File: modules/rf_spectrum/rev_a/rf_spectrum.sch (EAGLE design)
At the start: 38 parts, among them J1 MODULE_GENERIC_DEBUGSMT, J2 U.FL-R-SMT, J3 U.FL-R-SMT, J4 U.FL-R-SMT, J7 TC2030-JLINK-L, P1 MOLEX_73251-135X, U1 STM32L432KC, U2 MWSUB3G, U3 SKY13317, U7 TLV62130, X2 ABS05-32.768KHZ-9-T

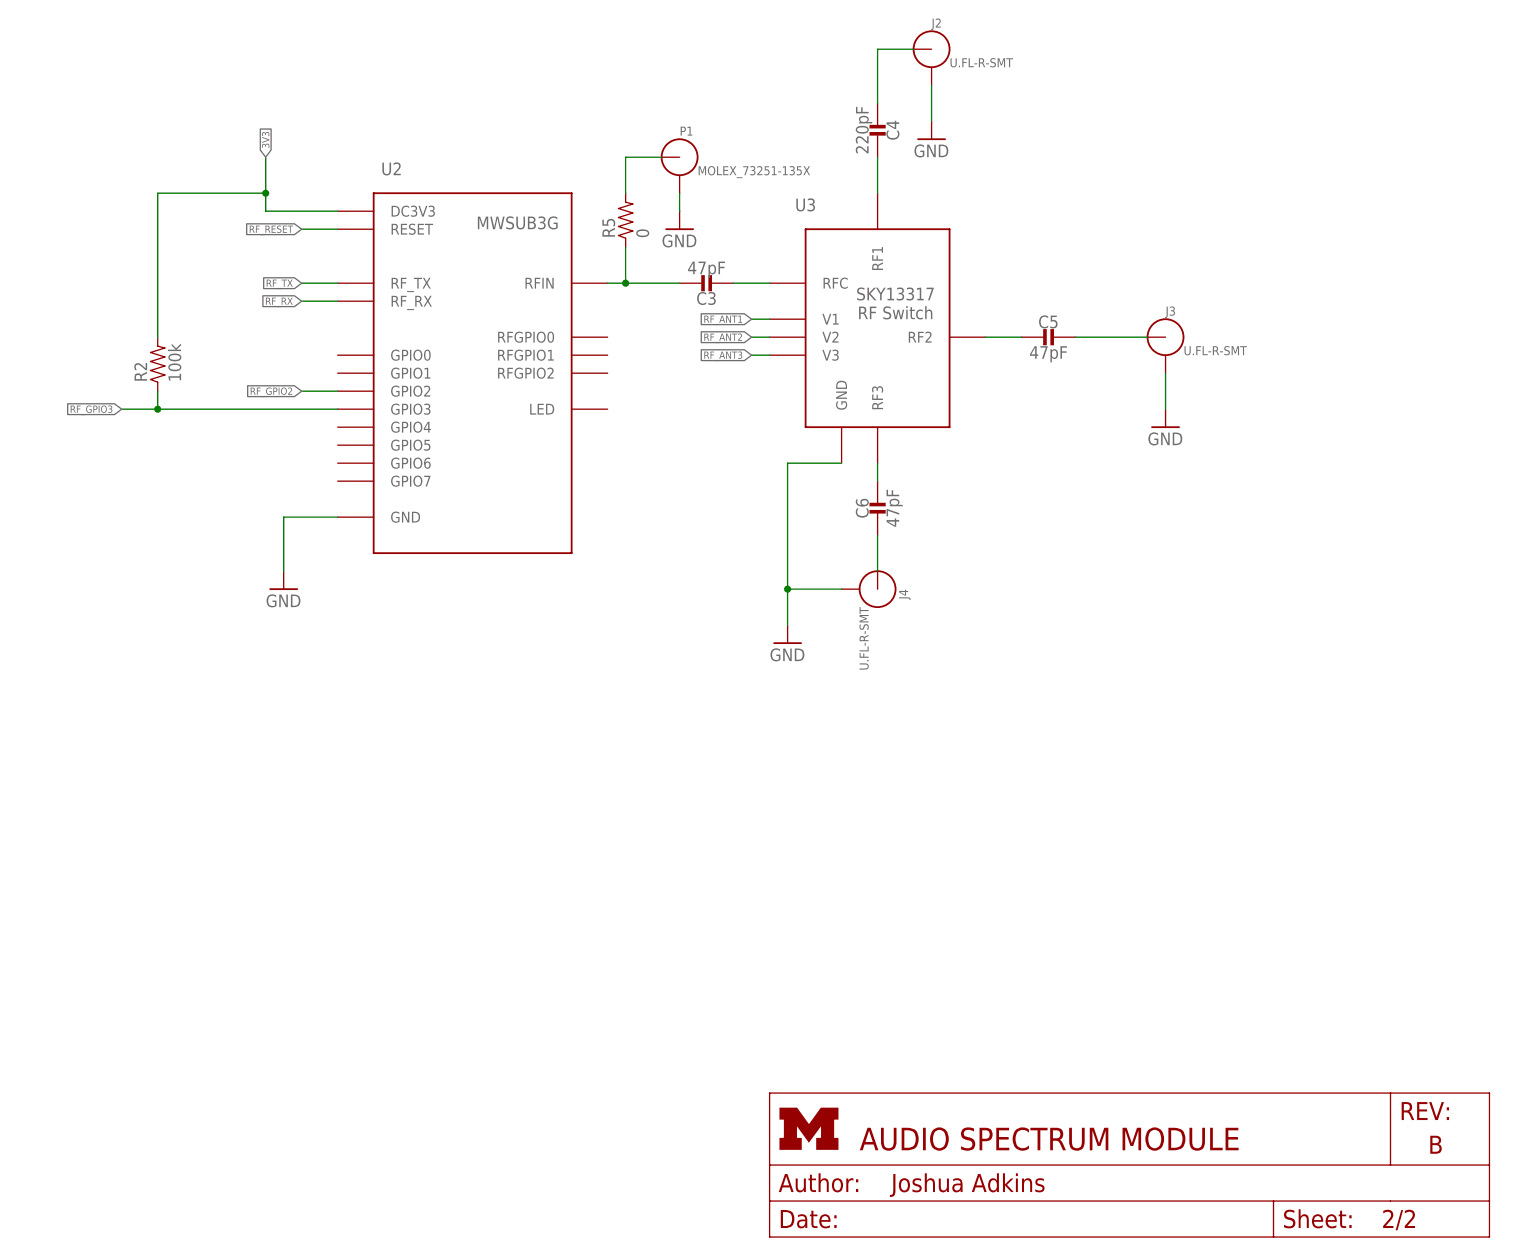
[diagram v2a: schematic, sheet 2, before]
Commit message: added debug signals and better labels
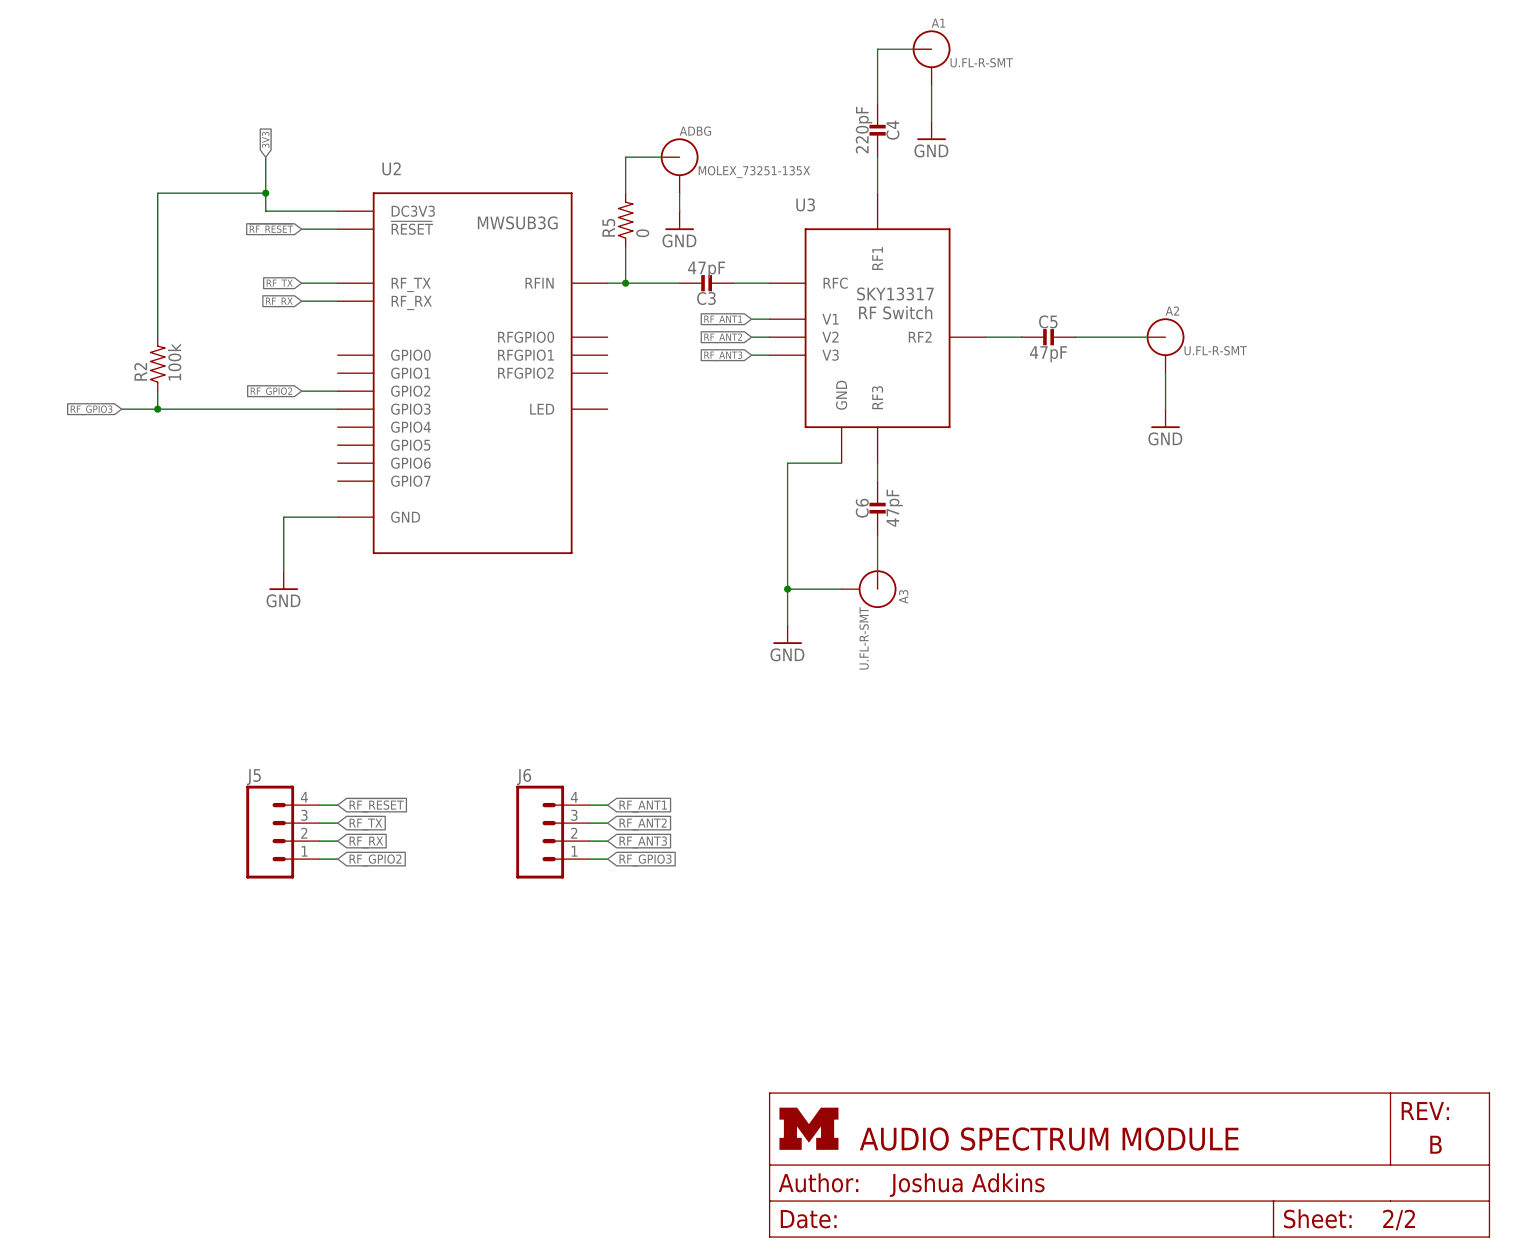
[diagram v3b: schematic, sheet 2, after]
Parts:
- added J5, J6: (no value), SparkFun-Connectors:M04PTH
- renumbered J2 to A1, J3 to A2, J4 to A3, P1 to ADBG
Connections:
- removed net RF_RESET: U1.PA8, U2.RESET
- new net !RF_RESET: J5.4, U1.PA8, U2.!RESET
- net RF_ANT1: now also J6.4
- net RF_ANT2: now also J6.3
- net RF_ANT3: now also J6.2
- net RF_GPIO2: now also J5.1
- net RF_GPIO3: now also J6.1
- net RF_RX: now also J5.2
- net RF_TX: now also J5.3
- net SWDCLK: now also U1.PA14/SWDCLK; no longer U1.PA14/SWCLK

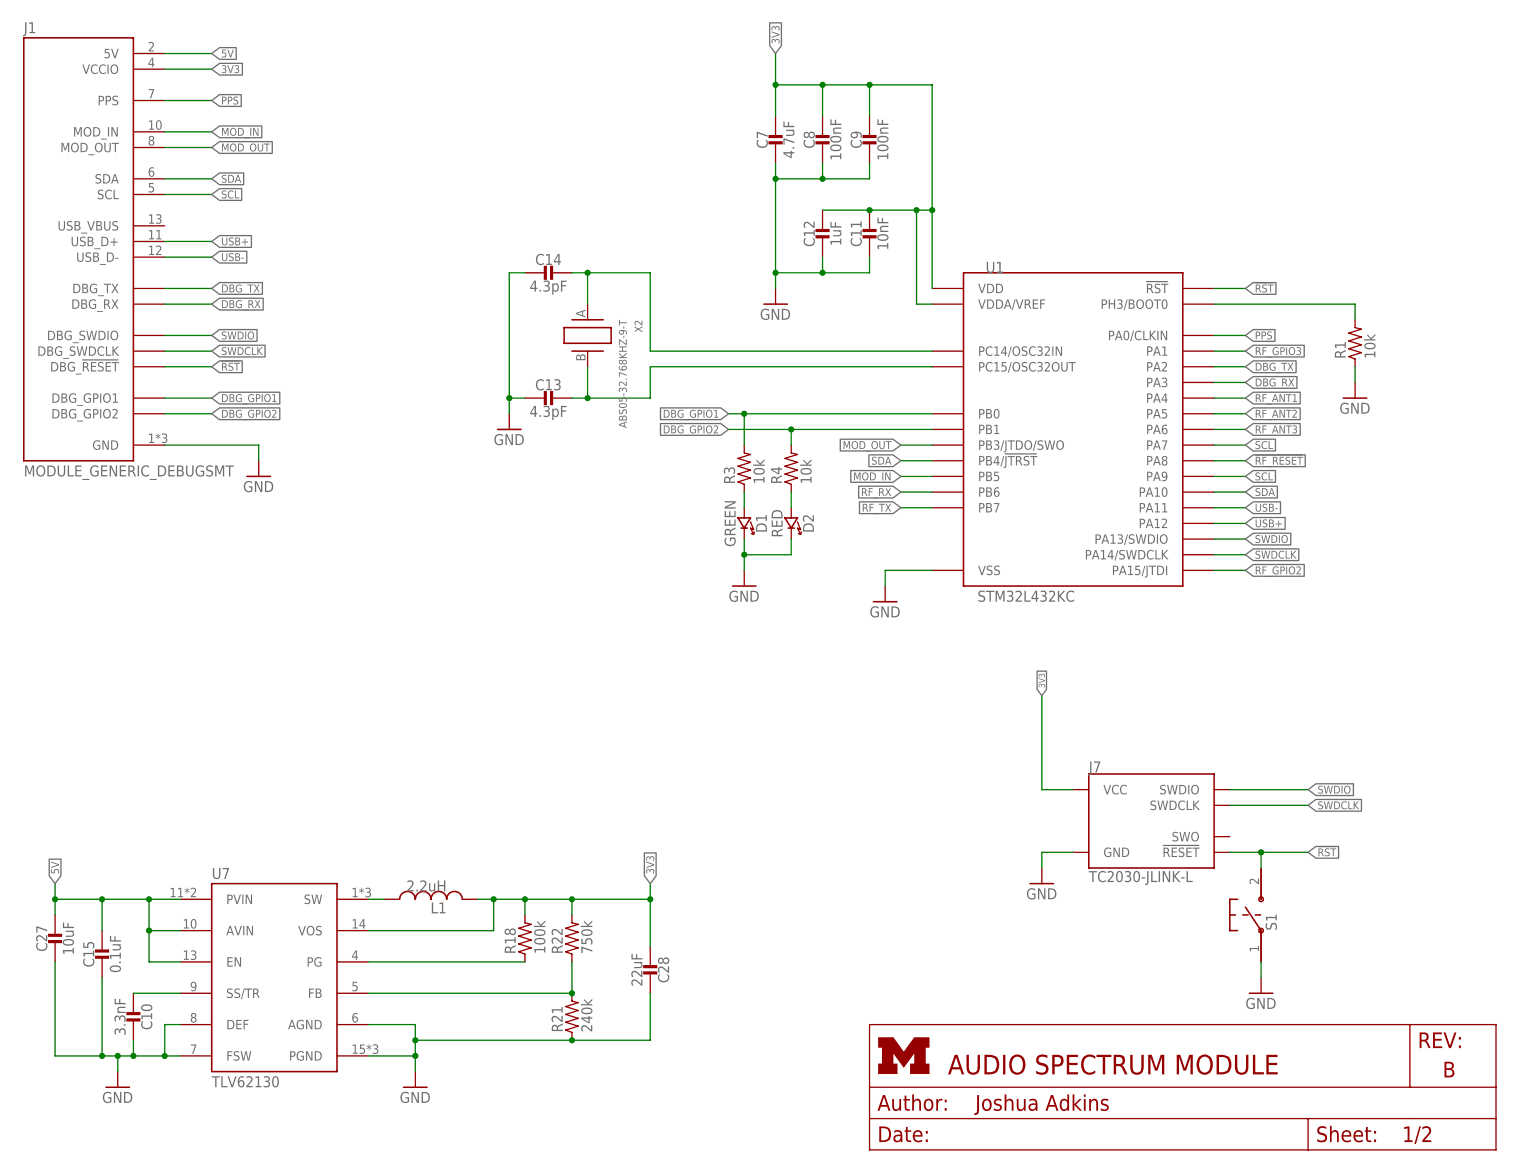
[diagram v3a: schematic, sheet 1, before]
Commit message: renumbered parts
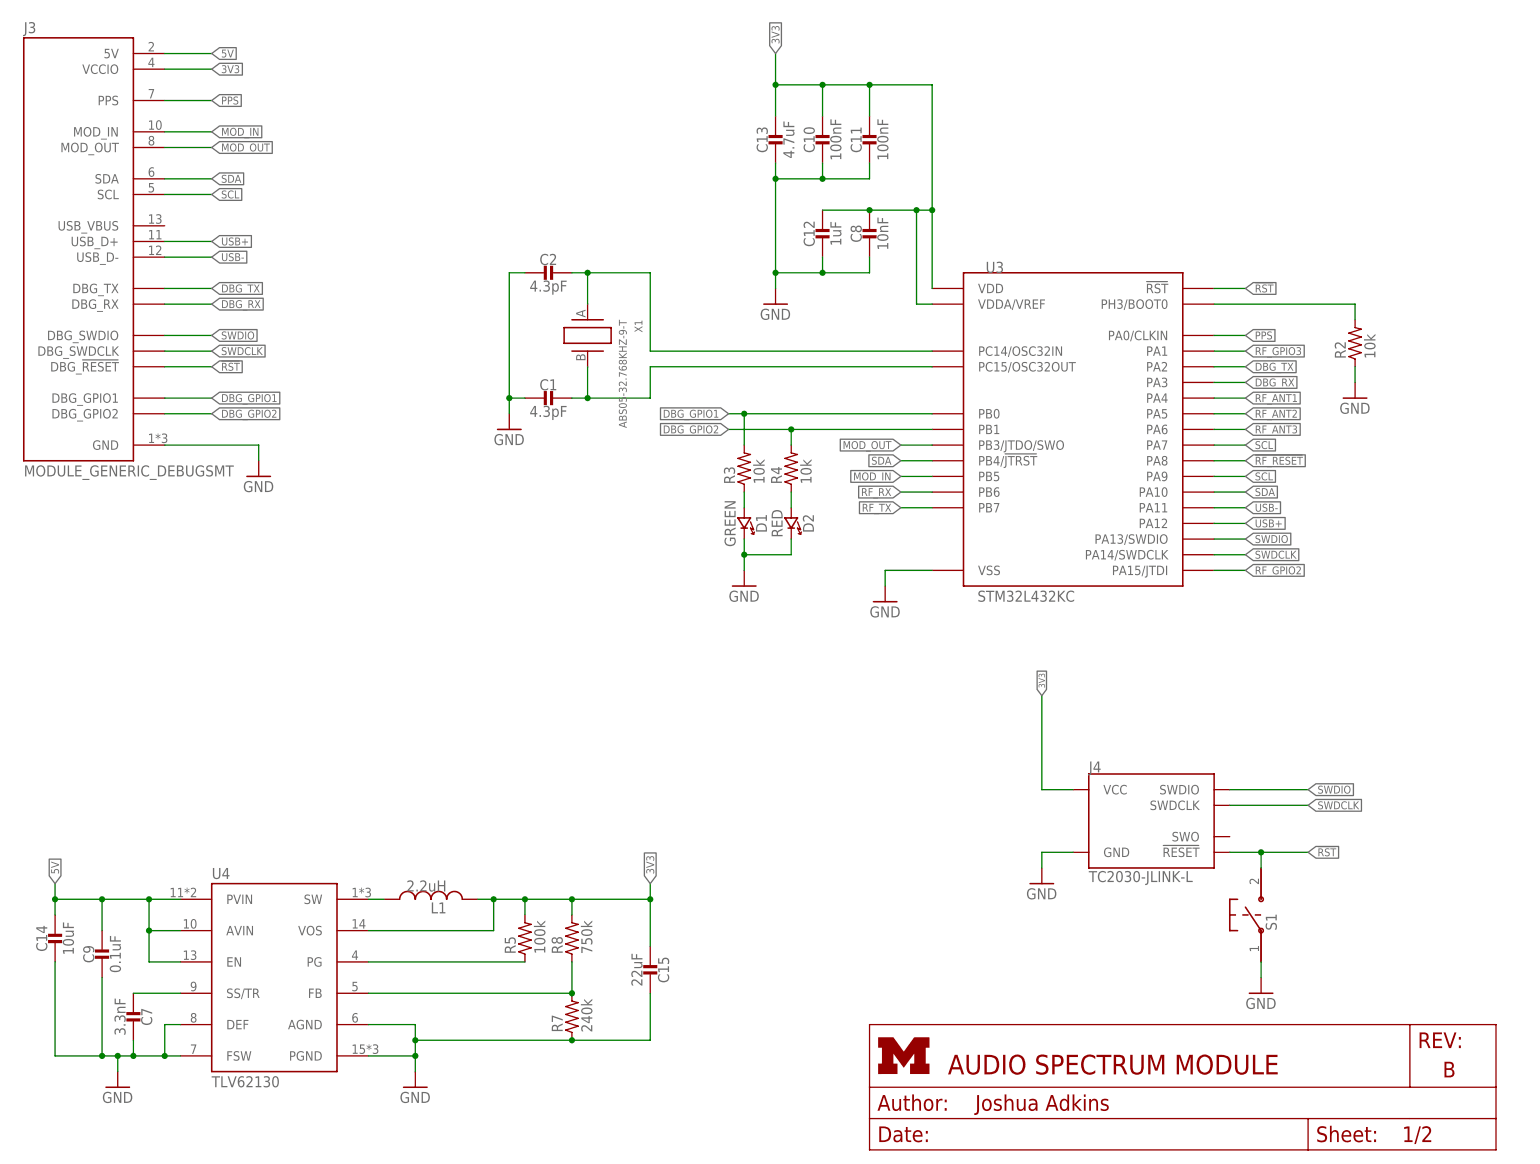
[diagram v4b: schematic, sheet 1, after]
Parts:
- removed C27: 10uF, passives:CAPACITOR0603_CAP
- removed C28: 22uF, passives:CAPACITOR0603_CAP
- removed J5: (no value), SparkFun-Connectors:M04PTH
- removed R18: 100k, passives:RESISTOR0603_RES
- added C1, C2: 4.3pF, passives:CAPACITOR0402_CAP
- added J3: MODULE_GENERIC_DEBUGSMT, signpost:MODULE_GENERIC_DEBUGSMT
- added R6: 100k, passives:RESISTOR0402_RES
- C10: value 3.3nF -> 100nF; device passives:CAPACITOR0603_CAP -> passives:CAPACITOR0402_CAP; DIGIKEY (none) -> 490-10777-1-ND
- C11: value 10nF -> 100nF
- C13: value 4.3pF -> 4.7uF; DIGIKEY 490-10777-1-ND -> 490-13252-1-ND
- C14: value 4.3pF -> 10uF; device passives:CAPACITOR0402_CAP -> passives:CAPACITOR0603_CAP; DIGIKEY 490-10777-1-ND -> (none)
- C15: value 0.1uF -> 22uF
- C4: value 220pF -> 47pF
- C6: value 47pF -> 220pF
- C7: value 4.7uF -> 3.3nF; device passives:CAPACITOR0402_CAP -> passives:CAPACITOR0603_CAP; DIGIKEY 490-13252-1-ND -> (none)
- C8: value 100nF -> 10nF
- C9: value 100nF -> 0.1uF; device passives:CAPACITOR0402_CAP -> passives:CAPACITOR0603_CAP; DIGIKEY 490-10777-1-ND -> (none)
- J1: value MODULE_GENERIC_DEBUGSMT -> (none); device signpost:MODULE_GENERIC_DEBUGSMT -> SparkFun-Connectors:M04PTH
- R1: value 10k -> 0
- R2: value 100k -> 10k
- R5: value 0 -> 100k; device passives:RESISTOR0402_RES -> passives:RESISTOR0603_RES
- U1: value STM32L432KC -> MWSUB3G; device chips:STM32L432KC -> signpost:MWSUB3G
- U2: value MWSUB3G -> SKY13317; device signpost:MWSUB3G -> chips:SKY13317
- U3: value SKY13317 -> STM32L432KC; device chips:SKY13317 -> chips:STM32L432KC
- renumbered J6 to J2, J7 to J4, R21 to R7, R22 to R8, U7 to U4, X2 to X1
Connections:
- net !RF_RESET: now also J1.4, U1.!RESET, U3.PA8; no longer J5.4, U1.PA8, U2.!RESET
- net !RST: now also J3.DBG_!RESET, U3.!RST; no longer J1.DBG_!RESET, U1.!RST
- net 3V3: now also C10.1, C13.1, C15.2, J3.VCCIO, R5.2, R6.2, U1.DC3V3, U3.VDD, U3.VDDA/VREF; no longer C28.2, C7.1, C9.1, J1.VCCIO, R18.2, R2.2, U1.VDD, U1.VDDA/VREF, U2.DC3V3
- net 5V: now also C14.1, C9.1, J3.5V; no longer C15.1, C27.1, J1.5V
- net DBG_GPIO1: now also J3.DBG_GPIO1, U3.PB0; no longer J1.DBG_GPIO1, U1.PB0
- net DBG_GPIO2: now also J3.DBG_GPIO2, U3.PB1; no longer J1.DBG_GPIO2, U1.PB1
- net DBG_RX: now also J3.DBG_RX, U3.PA3; no longer J1.DBG_RX, U1.PA3
- net DBG_TX: now also J3.DBG_TX, U3.PA2; no longer J1.DBG_TX, U1.PA2
- net GND: now also C1.2, C10.2, C15.1, C2.2, C7.1, J3.GND, R2.1, U1.GND, U3.VSS; no longer C10.1, C15.2, C27.2, C28.1, C7.2, J1.GND, R1.1, U1.VSS, U3.GND
- net MOD_IN: now also J3.MOD_IN, U3.PB5; no longer J1.MOD_IN, U1.PB5
- net MOD_OUT: now also J3.MOD_OUT, U3.PB3/JTDO/SWO; no longer J1.MOD_OUT, U1.PB3/JTDO/SWO
- net N$1: now also R1.1, U1.RFIN; no longer R5.1, U2.RFIN
- net N$10: now also C1.1, U3.PC15/OSC32OUT; no longer C13.1, U1.PC15/OSC32OUT
- net N$11: now also R2.2, U3.PH3/BOOT0; no longer R1.2, U1.PH3/BOOT0
- net N$14: now also R1.2; no longer R5.2
- net N$2: now also U2.RFC; no longer U3.RFC
- net N$3: now also C6.1, U2.RF1; no longer C4.1, U3.RF1
- net N$34: now also C7.2; no longer C10.2
- net N$36: now also R5.1; no longer R18.1
- net N$4: now also C6.2; no longer C4.2
- net N$5: now also C4.2, U2.RF2; no longer C5.2, U3.RF2
- net N$6: now also C4.1; no longer C5.1
- net N$7: now also C5.1, U2.RF3; no longer C6.1, U3.RF3
- net N$8: now also C5.2; no longer C6.2
- net N$9: now also C2.1, U3.PC14/OSC32IN; no longer C14.1, U1.PC14/OSC32IN
- net PPS: now also J3.PPS, U3.PA0/CLKIN; no longer J1.PPS, U1.PA0/CLKIN
- net RF_ANT1: now also U2.V1, U3.PA4; no longer U1.PA4, U3.V1
- net RF_ANT2: now also U2.V2, U3.PA5; no longer U1.PA5, U3.V2
- net RF_ANT3: now also U2.V3, U3.PA6; no longer U1.PA6, U3.V3
- net RF_GPIO2: now also J1.1, U1.GPIO2, U3.PA15/JTDI; no longer J5.1, U1.PA15/JTDI, U2.GPIO2
- net RF_GPIO3: now also R6.1, U1.GPIO3, U3.PA1; no longer R2.1, U1.PA1, U2.GPIO3
- net RF_RX: now also J1.2, U1.RF_RX, U3.PB6; no longer J5.2, U1.PB6, U2.RF_RX
- net RF_TX: now also J1.3, U1.RF_TX, U3.PB7; no longer J5.3, U1.PB7, U2.RF_TX
- net SCL: now also J3.SCL, U3.PA7, U3.PA9; no longer J1.SCL, U1.PA7, U1.PA9
- net SDA: now also J3.SDA, U3.PA10, U3.PB4/!JTRST; no longer J1.SDA, U1.PA10, U1.PB4/!JTRST
- net SWDCLK: now also J3.DBG_SWDCLK, U3.PA14/SWDCLK; no longer J1.DBG_SWDCLK, U1.PA14/SWDCLK
- net SWDIO: now also J3.DBG_SWDIO, U3.PA13/SWDIO; no longer J1.DBG_SWDIO, U1.PA13/SWDIO
- net USB+: now also J3.USB_D+, U3.PA12; no longer J1.USB_D+, U1.PA12
- net USB-: now also J3.USB_D-, U3.PA11; no longer J1.USB_D-, U1.PA11
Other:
- moved on the sheet: C10, C11, C13, C14, C15, C4, C5, C6, C7, C8, C9
